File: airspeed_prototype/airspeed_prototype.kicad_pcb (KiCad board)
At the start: 2 copper layers, 2 parts, among them U1 BME280, U2 ADXL343

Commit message: test
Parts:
- moved U2 9.18 mm to (134.6, 71.1)
- moved U1 5.98 mm to (141.2, 72.1), turned to -90 degrees
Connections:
- U1 pad 1: unconnected-(U1-GND-Pad1) -> GND
- U1 pad 7: unconnected-(U1-GND-Pad7) -> Net-(U1-GND-Pad7)
- U1 pad 8: unconnected-(U1-VDD-Pad8) -> +3.3V
- U2 pad 1: unconnected-(U2-Vdd_I/O-Pad1) -> +3.3V
- U2 pad 2: Net-(U2-GND-Pad2) -> Net-(U1-GND-Pad7)
- U2 pad 4: Net-(U2-GND-Pad2) -> Net-(U1-GND-Pad7)
- U2 pad 5: Net-(U2-GND-Pad2) -> Net-(U1-GND-Pad7)
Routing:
- net Net-(U1-GND-Pad7): track 0.00 -> 13.6 mm
- net +3.3V: track 0.00 -> 8.49 mm

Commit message: schematic
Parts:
- removed U1: BME280, Package_LGA:Bosch_LGA-8_2.5x2.5mm_P0.65mm_ClockwisePinNumbering
- removed U2: ADXL343, Package_LGA:LGA-14_3x5mm_P0.8mm_LayoutBorder1x6y
- added J1: Conn_01x03_Pin, Connector_PinHeader_2.54mm:PinHeader_1x03_P2.54mm_Vertical, F.Cu at (106.7, 61.0)
- added J2: Conn_01x10_Pin, Connector_PinHeader_2.54mm:PinHeader_1x10_P2.54mm_Vertical, F.Cu at (124.5, 66.0)
- added R1: 4k7, Resistor_SMD:R_0805_2012Metric, F.Cu at (115.9, 63.5)
- added R2: 10k, Resistor_SMD:R_0805_2012Metric, F.Cu at (115.9, 66.0)
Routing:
- net GND: track 0.00 -> 21.0 mm
- net Net-(U1-GND-Pad7): track 13.6 -> 0.00 mm
- net Net-(J2-Pin_2): track 0.00 -> 10.2 mm
- net +3.3V: track 8.49 -> 0.00 mm
- net Net-(J1-Pin_2): track 0.00 -> 8.33 mm
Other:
- board outline added: 29.2 x 34.3 mm

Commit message: update the schematic and pcb
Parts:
- removed J2: Conn_01x10_Pin, Connector_PinHeader_2.54mm:PinHeader_1x10_P2.54mm_Vertical
- added J3: Conn_01x06_Pin, Connector_PinHeader_2.54mm:PinHeader_1x06_P2.54mm_Vertical, F.Cu at (121.9, 68.6)
- added J4: Conn_01x08_Pin, Connector_PinHeader_2.54mm:PinHeader_1x08_P2.54mm_Vertical, F.Cu at (121.9, 46.0)
- added U1: ESP32-DevKitC, PCM_Espressif:ESP32-DevKitC, F.Cu at (89.2, 45.2)
- moved R1 32.7 mm to (83.7, 57.9)
- moved R2 31.4 mm to (84.8, 61.4), turned to -90 degrees
- moved J1 24.8 mm to (84.8, 72.6), turned to 180 degrees
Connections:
- J1 pad 1: +5V -> /5V
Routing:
- net /5V: track 0.00 -> 20.1 mm
- net GND: track 21.0 -> 39.6 mm
- net Net-(J1-Pin_2): track 8.33 -> 13.0 mm
- net Net-(U1-32K_XP/GPIO32/ADC1_CH4): track 10.2 -> 7.03 mm
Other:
- board size 29.2 x 34.3 mm -> 65.5 x 49.3 mm

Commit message: updates
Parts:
- moved J4 24.9 mm to (123.2, 70.9)
- moved J3 21.1 mm to (123.2, 47.5)
- moved J1 14.2 mm to (84.3, 86.9)
- moved R1 13.4 mm to (84.8, 71.2), turned to 90 degrees
- moved R2 2.75 mm to (84.8, 64.1)
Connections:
- net /5V renamed +5V
- J3 pad 1: unconnected-(J3-VCC-Pad1) -> +3.3V
- J3 pad 3: unconnected-(J3-SCL-Pad3) -> Net-(J3-SCL)
- J3 pad 4: unconnected-(J3-SDA-Pad4) -> Net-(J3-SDA)
- J4 pad 2: unconnected-(J4-VCC-Pad2) -> +3.3V
- J4 pad 4: unconnected-(J4-INT1-Pad4) -> Net-(J4-INT1)
- J4 pad 5: unconnected-(J4-INT2-Pad5) -> Net-(J4-INT2)
- J4 pad 7: unconnected-(J4-SDA-Pad7) -> Net-(J3-SDA)
- J4 pad 8: unconnected-(J4-SCL-Pad8) -> Net-(J3-SCL)
- U1 pad 1: /3.3V -> +3.3V
- U1 pad 23: unconnected-(U1-MTDO/GPIO15/ADC2_CH3-Pad23) -> Net-(J4-INT1)
- U1 pad 26: unconnected-(U1-ADC2_CH0/GPIO4-Pad26) -> Net-(J4-INT2)
- U1 pad 33: unconnected-(U1-GPIO21-Pad33) -> Net-(J3-SDA)
- U1 pad 36: unconnected-(U1-GPIO22-Pad36) -> Net-(J3-SCL)
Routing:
- net +3.3V: track 0.00 -> 81.1 mm
- net GND: track 39.6 -> 109.8 mm
- net Net-(J3-SCL): track 0.00 -> 51.3 mm
- net Net-(J3-SDA): track 0.00 -> 45.8 mm
- net +5V: track 20.1 -> 6.58 mm
- net Net-(J4-INT2): track 0.00 -> 10.8 mm
- net Net-(J4-INT1): track 0.00 -> 10.5 mm
- net Net-(U1-32K_XP/GPIO32/ADC1_CH4): track 7.03 -> 15.1 mm
- net Net-(J1-Pin_2): track 13.0 -> 13.6 mm
- net unconnected-(J4-CS-Pad3): track 0.00 -> 0.51 mm
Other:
- board size 65.5 x 49.3 mm -> 48.5 x 50.3 mm
- board text added: "velometa.com airspeed_board rev 1.0 2024-01-17"

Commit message: updates to pcb
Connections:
- net Net-(J3-SCL) renamed SCL
- net Net-(J3-SDA) renamed SDA
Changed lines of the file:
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@@
   (net 1 "Net-(J1-Pin_2)")
   (net 2 "GND")
-  (net 3 "Net-(J3-SCL)")
-  (net 4 "Net-(J3-SDA)")
+  (net 3 "SCL")
+  (net 4 "SDA")
   (net 5 "Net-(J4-INT1)")
   (net 6 "Net-(J4-INT2)")
@@
       (net 13 "unconnected-(J4-SDO-Pad6)") (pinfunction "SDO") (pintype "passive+no_connect"))
     (pad "7" thru_hole oval (at 0 15.24) (size 1.7 1.7) (drill 1) (layers "*.Cu" "*.Mask")
-      (net 4 "Net-(J3-SDA)") (pinfunction "SDA") (pintype "passive"))
+      (net 4 "SDA") (pinfunction "SDA") (pintype "passive"))
     (pad "8" thru_hole oval (at 0 17.78) (size 1.7 1.7) (drill 1) (layers "*.Cu" "*.Mask")
-      (net 3 "Net-(J3-SCL)") (pinfunction "SCL") (pintype "passive"))
+      (net 3 "SCL") (pinfunction "SCL") (pintype "passive"))
     (model "${KICAD6_3DMODEL_DIR}/Connector_PinHeader_2.54mm.3dshapes/PinHeader_1x08_P2.54mm_Vertical.wrl"
       (offset (xyz 0 0 0))
@@
       (net 2 "GND") (pinfunction "GND") (pintype "passive"))
     (pad "33" thru_hole oval (at 25.4 12.7 270) (size 1.2 2) (drill 0.8) (layers "*.Cu" "*.Mask")
-      (net 4 "Net-(J3-SDA)") (pinfunction "SDA") (pintype "bidirectional"))
+      (net 4 "SDA") (pinfunction "SDA") (pintype "bidirectional"))
     (pad "34" thru_hole oval (at 25.4 10.16 270) (size 1.2 2) (drill 0.8) (layers "*.Cu" "*.Mask")
       (net 39 "unconnected-(U1-U0RXD{slash}GPIO3-Pad34)") (pinfunction "U0RXD/GPIO3") (pintype "bidirectional+no_connect"))
@@
       (net 40 "unconnected-(U1-U0TXD{slash}GPIO1-Pad35)") (pinfunction "U0TXD/GPIO1") (pintype "bidirectional+no_connect"))
     (pad "36" thru_hole oval (at 25.4 5.08 270) (size 1.2 2) (drill 0.8) (layers "*.Cu" "*.Mask")
-      (net 3 "Net-(J3-SCL)") (pinfunction "SCL") (pintype "bidirectional"))
+      (net 3 "SCL") (pinfunction "SCL") (pintype "bidirectional"))
     (pad "37" thru_hole oval (at 25.4 2.54 270) (size 1.2 2) (drill 0.8) (layers "*.Cu" "*.Mask")
       (net 41 "unconnected-(U1-GPIO23-Pad37)") (pinfunction "GPIO23") (pintype "bidirectional+no_connect"))
@@
       (net 2 "GND") (pinfunction "GND") (pintype "passive"))
     (pad "3" thru_hole oval (at 0 5.08) (size 1.7 1.7) (drill 1) (layers "*.Cu" "*.Mask")
-      (net 3 "Net-(J3-SCL)") (pinfunction "SCL") (pintype "passive"))
+      (net 3 "SCL") (pinfunction "SCL") (pintype "passive"))
     (pad "4" thru_hole oval (at 0 7.62) (size 1.7 1.7) (drill 1) (layers "*.Cu" "*.Mask")
-      (net 4 "Net-(J3-SDA)") (pinfunction "SDA") (pintype "passive"))
+      (net 4 "SDA") (pinfunction "SDA") (pintype "passive"))
     (pad "5" thru_hole oval (at 0 10.16) (size 1.7 1.7) (drill 1) (layers "*.Cu" "*.Mask")
       (net 10 "unconnected-(J3-CSB-Pad5)") (pinfunction "CSB") (pintype "passive+no_connect"))

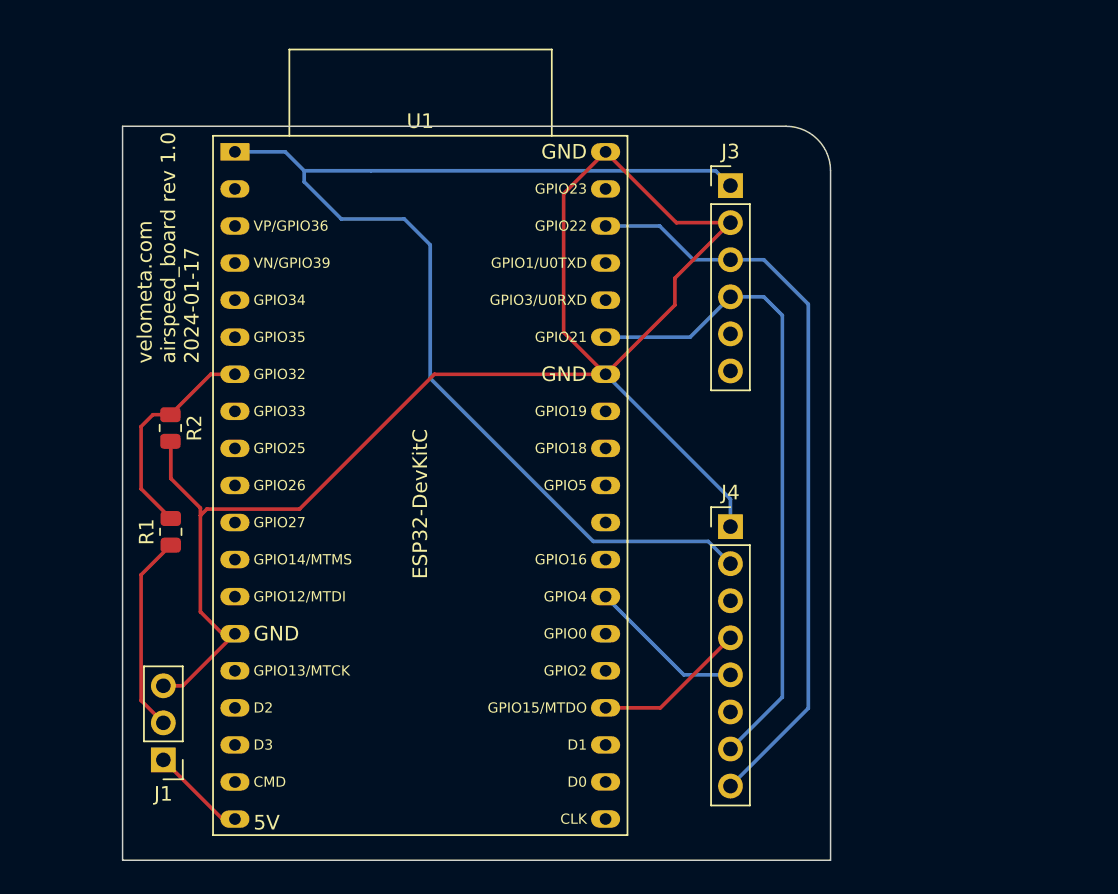
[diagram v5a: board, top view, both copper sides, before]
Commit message: new pcb layout
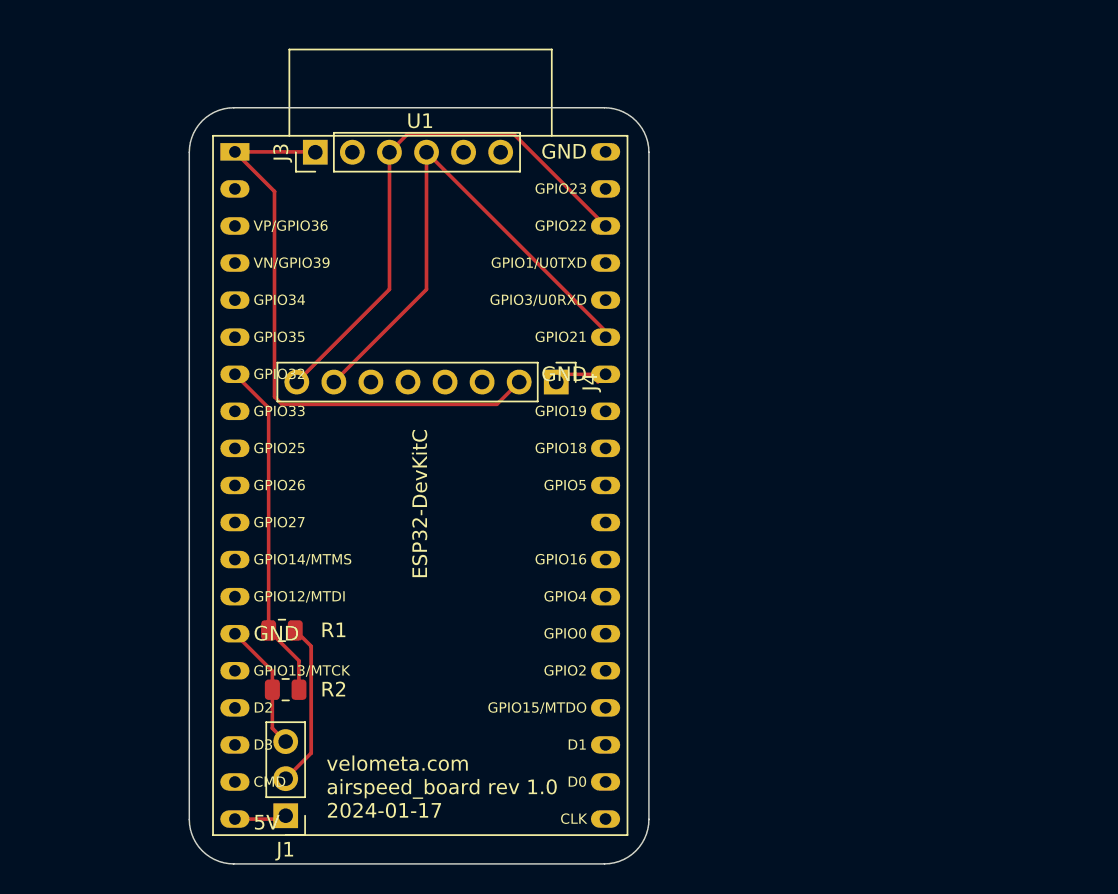
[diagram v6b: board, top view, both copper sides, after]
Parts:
- moved J3 28.5 mm to (94.7, 45.2), turned to 90 degrees
- moved R2 19.6 mm to (92.7, 82.0), turned to 180 degrees
- moved J4 15.5 mm to (111.3, 61.0), turned to -90 degrees
- moved R1 10.2 mm to (92.5, 78.0), turned to 180 degrees
- moved J1 9.21 mm to (92.7, 90.7)
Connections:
- J4 pad 4: Net-(J4-INT1) -> unconnected-(J4-INT1-Pad4)
- J4 pad 5: Net-(J4-INT2) -> unconnected-(J4-INT2-Pad5)
- U1 pad 23: Net-(J4-INT1) -> unconnected-(U1-MTDO/GPIO15/ADC2_CH3-Pad23)
- U1 pad 26: Net-(J4-INT2) -> unconnected-(U1-ADC2_CH0/GPIO4-Pad26)
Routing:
- net GND: track 109.8 -> 14.1 mm
- net +3.3V: track 81.1 -> 41.0 mm
- net SCL: track 51.3 -> 36.3 mm
- net Net-(J4-INT2): track 10.8 -> 0.00 mm
- net Net-(J4-INT1): track 10.5 -> 0.00 mm
- net SDA: track 45.8 -> 36.9 mm
- net Net-(U1-32K_XP/GPIO32/ADC1_CH4): track 15.1 -> 23.4 mm
- net Net-(J1-Pin_2): track 13.6 -> 11.3 mm
- net +5V: track 6.58 -> 4.75 mm
- net unconnected-(J4-CS-Pad3): track 0.51 -> 0.00 mm
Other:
- board size 48.5 x 50.3 mm -> 31.5 x 51.8 mm
- board text added: "Conn_01x08_Pin"

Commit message: updates to pcb
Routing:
- net GND: track 14.1 -> 32.8 mm
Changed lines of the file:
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@@
   (segment (start 94.46 86.388) (end 92.71 88.138) (width 0.25) (layer "F.Cu") (net 1))
   (segment (start 88.36612 78.20612) (end 89.2325 78.20612) (width 0.25) (layer "F.Cu") (net 2))
+  (segment (start 99.002 43.492) (end 112.93838 43.492) (width 0.25) (layer "F.Cu") (net 2))
   (segment (start 91.7975 80.77112) (end 89.2325 78.20612) (width 0.25) (layer "F.Cu") (net 2))
   (segment (start 114.6325 60.42612) (end 111.78588 60.42612) (width 0.25) (layer "F.Cu") (net 2))
+  (segment (start 112.93838 43.492) (end 114.6325 45.18612) (width 0.25) (layer "F.Cu") (net 2))
   (segment (start 91.7975 82.042) (end 91.7975 80.77112) (width 0.25) (layer "F.Cu") (net 2))
+  (segment (start 97.282 45.212) (end 99.002 43.492) (width 0.25) (layer "F.Cu") (net 2))
   (segment (start 91.7975 84.6855) (end 92.71 85.598) (width 0.25) (layer "F.Cu") (net 2))
   (segment (start 91.7975 82.042) (end 91.7975 84.6855) (width 0.25) (layer "F.Cu") (net 2))
